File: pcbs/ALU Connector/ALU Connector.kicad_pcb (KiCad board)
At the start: 2 copper layers, 4 parts, among them J101 Conn_02x20_Odd_Even, J102 Conn_02x20_Odd_Even, J103 Conn_01x04, J104 Conn_02x20_Odd_Even

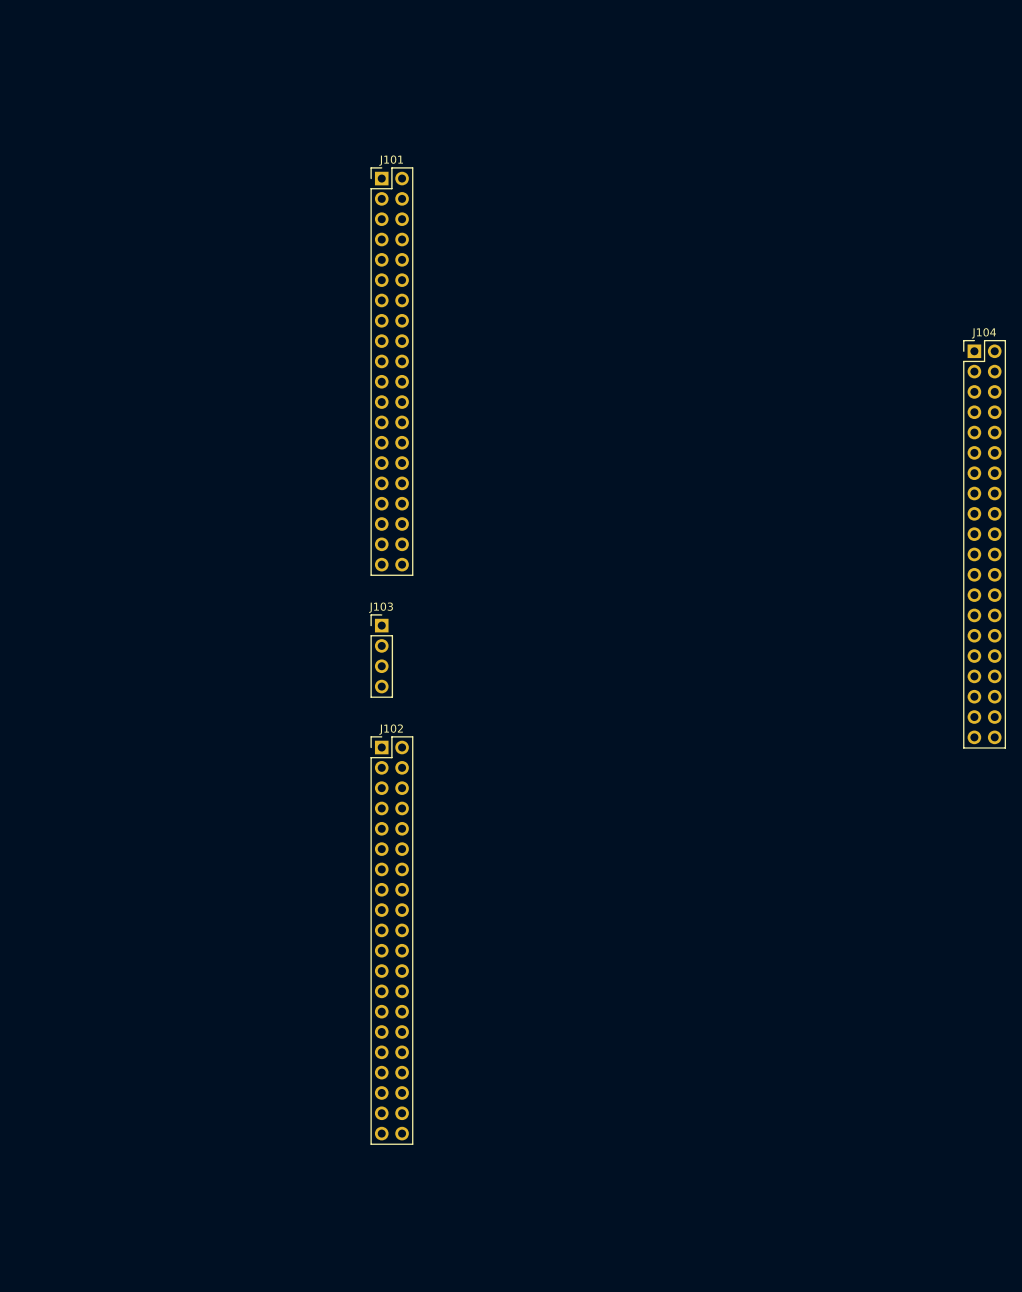
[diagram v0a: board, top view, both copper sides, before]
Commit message: Some basic routing
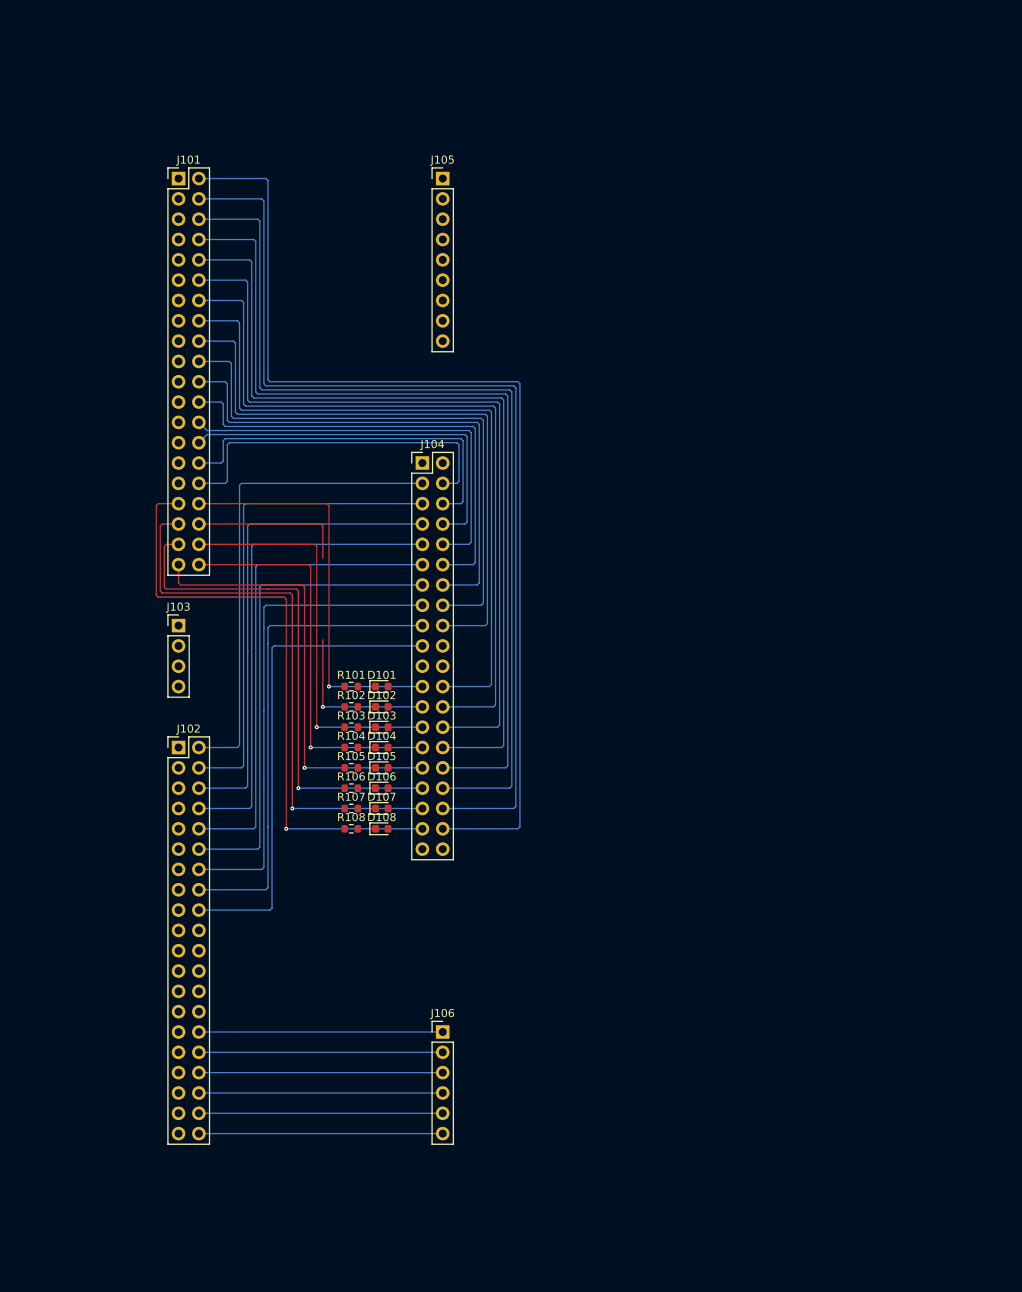
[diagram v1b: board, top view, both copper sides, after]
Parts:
- added D101: Blue, LED_SMD:LED_0603_1608Metric, F.Cu at (76.2, 114.3)
- added D102: Blue, LED_SMD:LED_0603_1608Metric, F.Cu at (76.2, 116.8)
- added D103: Blue, LED_SMD:LED_0603_1608Metric, F.Cu at (76.2, 119.4)
- added D104: Blue, LED_SMD:LED_0603_1608Metric, F.Cu at (76.2, 121.9)
- added D105: Blue, LED_SMD:LED_0603_1608Metric, F.Cu at (76.2, 124.5)
- added D106: Blue, LED_SMD:LED_0603_1608Metric, F.Cu at (76.2, 127.0)
- added D107: Blue, LED_SMD:LED_0603_1608Metric, F.Cu at (76.2, 129.5)
- added D108: Blue, LED_SMD:LED_0603_1608Metric, F.Cu at (76.2, 132.1)
- added J105: Conn_01x09, Connector_PinHeader_2.54mm:PinHeader_1x09_P2.54mm_Vertical, F.Cu at (83.8, 50.8)
- added J106: Conn_01x06, Connector_PinHeader_2.54mm:PinHeader_1x06_P2.54mm_Vertical, F.Cu at (83.8, 157.5)
- added R101: 4k7, Resistor_SMD:R_0603_1608Metric, F.Cu at (72.4, 114.3)
- added R102: 4k7, Resistor_SMD:R_0603_1608Metric, F.Cu at (72.4, 116.8)
- added R103: 4k7, Resistor_SMD:R_0603_1608Metric, F.Cu at (72.4, 119.4)
- added R104: 4k7, Resistor_SMD:R_0603_1608Metric, F.Cu at (72.4, 121.9)
- added R105: 4k7, Resistor_SMD:R_0603_1608Metric, F.Cu at (72.4, 124.5)
- added R106: 4k7, Resistor_SMD:R_0603_1608Metric, F.Cu at (72.4, 127.0)
- added R107: 4k7, Resistor_SMD:R_0603_1608Metric, F.Cu at (72.4, 129.5)
- added R108: 4k7, Resistor_SMD:R_0603_1608Metric, F.Cu at (72.4, 132.1)
- moved J104 70.4 mm to (81.3, 86.4)
- moved J101 25.4 mm to (50.8, 50.8)
- moved J102 25.4 mm to (50.8, 121.9)
- moved J103 25.4 mm to (50.8, 106.7)
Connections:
- J101 pad 10: /A_{4} -> /B_{3}
- J101 pad 12: /A_{5} -> /B_{2}
- J101 pad 14: /A_{6} -> /B_{1}
- J101 pad 16: /A_{7} -> /B_{0}
- J101 pad 18: /B_{0} -> /A_{7}
- J101 pad 2: /A_{0} -> /B_{7}
- J101 pad 20: /B_{1} -> /A_{6}
- J101 pad 22: /B_{2} -> /A_{5}
- J101 pad 24: /B_{3} -> /A_{4}
- J101 pad 26: /B_{4} -> /A_{3}
- J101 pad 28: /B_{5} -> /A_{2}
- J101 pad 30: /B_{6} -> /A_{1}
- J101 pad 32: /B_{7} -> /A_{0}
- J101 pad 33: unconnected-(J101-Pad33) -> /Commit
- J101 pad 34: unconnected-(J101-Pad34) -> /I_{0}
- J101 pad 35: unconnected-(J101-Pad35) -> /Execute
- J101 pad 36: unconnected-(J101-Pad36) -> /I_{1}
- J101 pad 37: unconnected-(J101-Pad37) -> /Decode
- J101 pad 38: unconnected-(J101-Pad38) -> /I_{2}
- J101 pad 39: unconnected-(J101-Pad39) -> /~{SELECT}
- J101 pad 4: /A_{1} -> /B_{6}
- J101 pad 40: unconnected-(J101-Pad40) -> /I_{3}
- J101 pad 6: /A_{2} -> /B_{5}
- J101 pad 8: /A_{3} -> /B_{4}
- J102 pad 1: unconnected-(J102-Pad1) -> /Result_{0}
- J102 pad 10: unconnected-(J102-Pad10) -> /C_{4}
- J102 pad 11: unconnected-(J102-Pad11) -> /Result_{5}
- J102 pad 12: unconnected-(J102-Pad12) -> /C_{5}
- J102 pad 13: unconnected-(J102-Pad13) -> /Result_{6}
- J102 pad 14: unconnected-(J102-Pad14) -> /C_{6}
- J102 pad 15: unconnected-(J102-Pad15) -> /Result_{7}
- J102 pad 16: unconnected-(J102-Pad16) -> /C_{7}
- J102 pad 17: unconnected-(J102-Pad17) -> /Flag
- J102 pad 18: unconnected-(J102-Pad18) -> /DALU_{flag}
- J102 pad 2: unconnected-(J102-Pad2) -> /C_{0}
- J102 pad 3: unconnected-(J102-Pad3) -> /Result_{1}
- J102 pad 30: unconnected-(J102-Pad30) -> /NAND
- J102 pad 32: unconnected-(J102-Pad32) -> /AND
- J102 pad 34: unconnected-(J102-Pad34) -> /XOR
- J102 pad 36: unconnected-(J102-Pad36) -> /OR
- J102 pad 38: unconnected-(J102-Pad38) -> /SUB
- J102 pad 4: unconnected-(J102-Pad4) -> /C_{1}
- J102 pad 40: unconnected-(J102-Pad40) -> /ADD
- J102 pad 5: unconnected-(J102-Pad5) -> /Result_{2}
- J102 pad 6: unconnected-(J102-Pad6) -> /C_{2}
- J102 pad 7: unconnected-(J102-Pad7) -> /Result_{3}
- J102 pad 8: unconnected-(J102-Pad8) -> /C_{3}
- J102 pad 9: unconnected-(J102-Pad9) -> /Result_{4}
- J104 pad 19: unconnected-(J104-Pad19) -> /DALU_{flag}
- J104 pad 23: unconnected-(J104-Pad23) -> /I_{0}
- J104 pad 25: unconnected-(J104-Pad25) -> /I_{1}
- J104 pad 27: unconnected-(J104-Pad27) -> /I_{2}
- J104 pad 29: unconnected-(J104-Pad29) -> /I_{3}
- J104 pad 31: unconnected-(J104-Pad31) -> /~{SELECT}
- J104 pad 33: unconnected-(J104-Pad33) -> /Decode
- J104 pad 35: unconnected-(J104-Pad35) -> /Execute
- J104 pad 37: unconnected-(J104-Pad37) -> /Commit
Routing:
- net /B_{7}: track 0.00 -> 130.5 mm
- net /B_{6}: track 0.00 -> 124.4 mm
- net /B_{5}: track 0.00 -> 118.3 mm
- net /B_{4}: track 0.00 -> 112.2 mm
- net /B_{3}: track 0.00 -> 106.1 mm
- net /B_{2}: track 0.00 -> 100.0 mm
- net /B_{1}: track 0.00 -> 93.9 mm
- net /B_{0}: track 0.00 -> 87.8 mm
- net /A_{7}: track 0.00 -> 76.6 mm
- net /Commit: track 0.00 -> 76.3 mm, vias 0 -> 1
- net /A_{6}: track 0.00 -> 70.5 mm
- net /Execute: track 0.00 -> 70.2 mm, vias 0 -> 1
- net /A_{5}: track 0.00 -> 64.4 mm
- net /Decode: track 0.00 -> 64.1 mm, vias 0 -> 1
- net /C_{2}: track 0.00 -> 60.9 mm
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
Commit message: More routing and LEDs
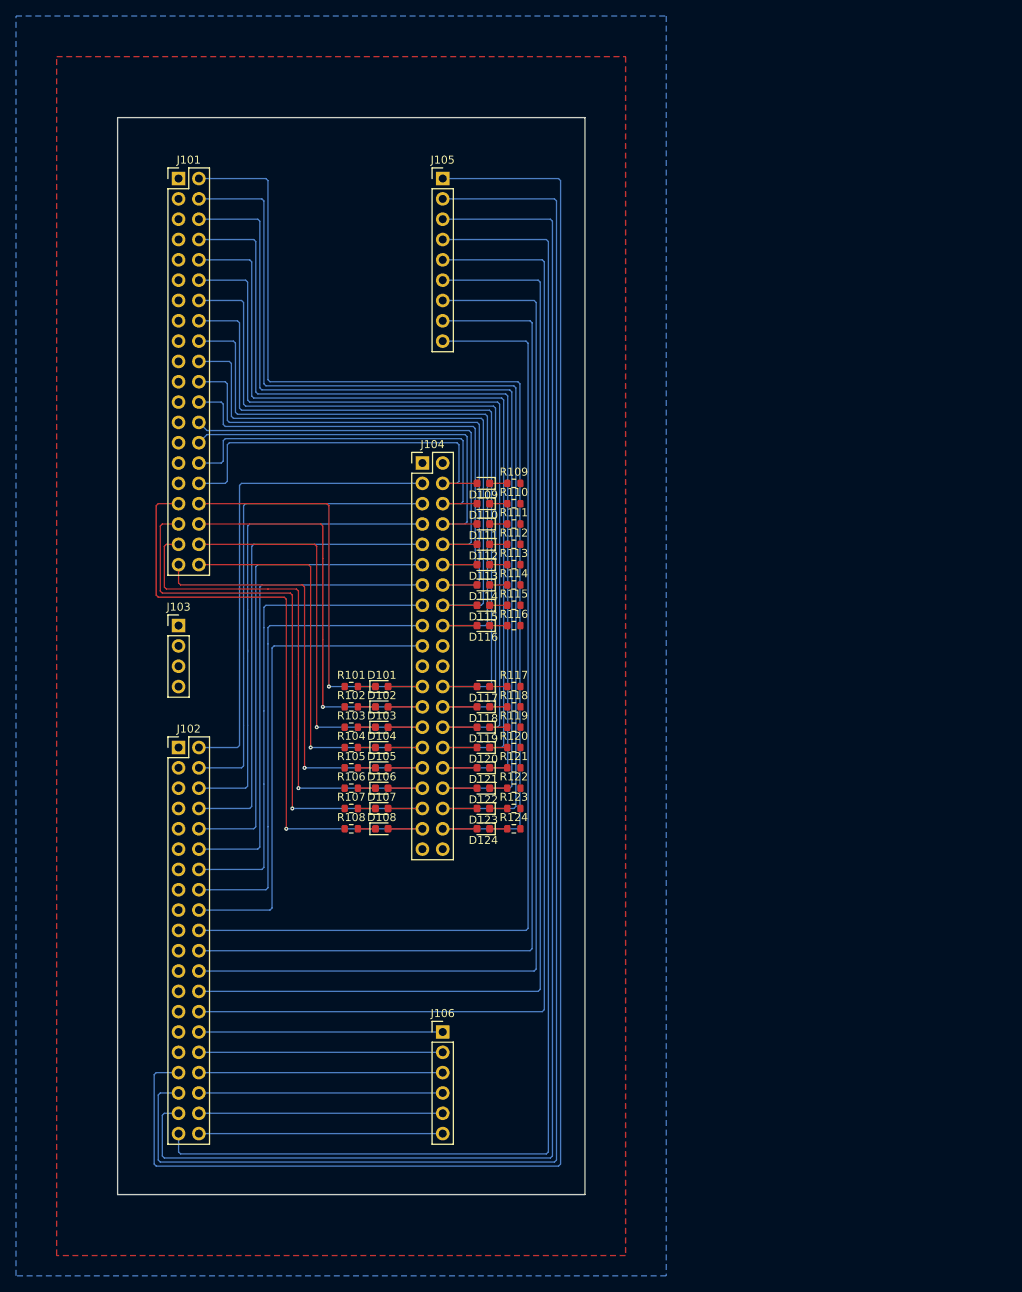
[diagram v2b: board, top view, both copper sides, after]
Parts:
- added D109: Green, LED_SMD:LED_0603_1608Metric, F.Cu at (88.9, 88.9)
- added D110: Green, LED_SMD:LED_0603_1608Metric, F.Cu at (88.9, 91.4)
- added D111: Green, LED_SMD:LED_0603_1608Metric, F.Cu at (88.9, 94.0)
- added D112: Green, LED_SMD:LED_0603_1608Metric, F.Cu at (88.9, 96.5)
- added D113: Green, LED_SMD:LED_0603_1608Metric, F.Cu at (88.9, 99.1)
- added D114: Green, LED_SMD:LED_0603_1608Metric, F.Cu at (88.9, 101.6)
- added D115: Green, LED_SMD:LED_0603_1608Metric, F.Cu at (88.9, 104.1)
- added D116: Green, LED_SMD:LED_0603_1608Metric, F.Cu at (88.9, 106.7)
- added D117: Green, LED_SMD:LED_0603_1608Metric, F.Cu at (88.9, 114.3)
- added D118: Green, LED_SMD:LED_0603_1608Metric, F.Cu at (88.9, 116.8)
- added D119: Green, LED_SMD:LED_0603_1608Metric, F.Cu at (88.9, 119.4)
- added D120: Green, LED_SMD:LED_0603_1608Metric, F.Cu at (88.9, 121.9)
- added D121: Green, LED_SMD:LED_0603_1608Metric, F.Cu at (88.9, 124.5)
- added D122: Green, LED_SMD:LED_0603_1608Metric, F.Cu at (88.9, 127.0)
- added D123: Green, LED_SMD:LED_0603_1608Metric, F.Cu at (88.9, 129.5)
- added D124: Green, LED_SMD:LED_0603_1608Metric, F.Cu at (88.9, 132.1)
- added R109: 4k7, Resistor_SMD:R_0603_1608Metric, F.Cu at (92.7, 88.9)
- added R110: 4k7, Resistor_SMD:R_0603_1608Metric, F.Cu at (92.7, 91.4)
- added R111: 4k7, Resistor_SMD:R_0603_1608Metric, F.Cu at (92.7, 94.0)
- added R112: 4k7, Resistor_SMD:R_0603_1608Metric, F.Cu at (92.7, 96.5)
- added R113: 4k7, Resistor_SMD:R_0603_1608Metric, F.Cu at (92.7, 99.1)
- added R114: 4k7, Resistor_SMD:R_0603_1608Metric, F.Cu at (92.7, 101.6)
- added R115: 4k7, Resistor_SMD:R_0603_1608Metric, F.Cu at (92.7, 104.1)
- added R116: 4k7, Resistor_SMD:R_0603_1608Metric, F.Cu at (92.7, 106.7)
- added R117: 4k7, Resistor_SMD:R_0603_1608Metric, F.Cu at (92.7, 114.3)
- added R118: 4k7, Resistor_SMD:R_0603_1608Metric, F.Cu at (92.7, 116.8)
- added R119: 4k7, Resistor_SMD:R_0603_1608Metric, F.Cu at (92.7, 119.4)
- added R120: 4k7, Resistor_SMD:R_0603_1608Metric, F.Cu at (92.7, 121.9)
- added R121: 4k7, Resistor_SMD:R_0603_1608Metric, F.Cu at (92.7, 124.5)
- added R122: 4k7, Resistor_SMD:R_0603_1608Metric, F.Cu at (92.7, 127.0)
- added R123: 4k7, Resistor_SMD:R_0603_1608Metric, F.Cu at (92.7, 129.5)
- added R124: 4k7, Resistor_SMD:R_0603_1608Metric, F.Cu at (92.7, 132.1)
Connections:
- J102 pad 1: /Result_{0} -> unconnected-(J102-Pad1)
- J102 pad 11: /Result_{5} -> unconnected-(J102-Pad11)
- J102 pad 13: /Result_{6} -> unconnected-(J102-Pad13)
- J102 pad 15: /Result_{7} -> unconnected-(J102-Pad15)
- J102 pad 17: /Flag -> unconnected-(J102-Pad17)
- J102 pad 20: unconnected-(J102-Pad20) -> /Flag
- J102 pad 22: unconnected-(J102-Pad22) -> /Result_{7}
- J102 pad 24: unconnected-(J102-Pad24) -> /Result_{6}
- J102 pad 26: unconnected-(J102-Pad26) -> /Result_{5}
- J102 pad 28: unconnected-(J102-Pad28) -> /Result_{4}
- J102 pad 3: /Result_{1} -> unconnected-(J102-Pad3)
- J102 pad 33: unconnected-(J102-Pad33) -> /Result_{0}
- J102 pad 35: unconnected-(J102-Pad35) -> /Result_{1}
- J102 pad 37: unconnected-(J102-Pad37) -> /Result_{2}
- J102 pad 39: unconnected-(J102-Pad39) -> /Result_{3}
- J102 pad 5: /Result_{2} -> unconnected-(J102-Pad5)
- J102 pad 7: /Result_{3} -> unconnected-(J102-Pad7)
- J102 pad 9: /Result_{4} -> unconnected-(J102-Pad9)
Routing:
- net /Result_{0}: track 0.00 -> 203.1 mm
- net /Result_{1}: track 0.00 -> 195.0 mm
- net /Result_{2}: track 0.00 -> 186.9 mm
- net /Result_{3}: track 0.00 -> 175.8 mm
- net /Result_{4}: track 0.00 -> 149.6 mm
- net /Result_{5}: track 0.00 -> 143.5 mm
- net /Result_{6}: track 0.00 -> 137.4 mm
- net /Result_{7}: track 0.00 -> 131.3 mm
- net /Flag: track 0.00 -> 125.2 mm
- net /I_{1}: track 40.5 -> 54.9 mm
- net /Decode: track 64.1 -> 68.4 mm
- net /B_{7}: track 130.5 -> 134.8 mm
- net /~{SELECT}: track 55.6 -> 59.9 mm
- net /I_{3}: track 50.7 -> 54.9 mm
- net /I_{2}: track 50.7 -> 54.9 mm
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- added copper zone on B.Cu, net +5V
- added copper zone on F.Cu, net GND
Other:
- board outline added: 58.4 x 134.6 mm

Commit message: Realised a mistake
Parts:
- added J107: Conn_01x10, Connector_PinHeader_2.54mm:PinHeader_1x10_P2.54mm_Vertical, F.Cu at (63.5, 170.2)
- J105: value Conn_01x09 -> Conn_01x10; footprint Connector_PinHeader_2.54mm:PinHeader_1x09_P2.54mm_Vertical -> Connector_PinHeader_2.54mm:PinHeader_1x10_P2.54mm_Vertical
- J106: value Conn_01x06 -> Conn_01x10; footprint Connector_PinHeader_2.54mm:PinHeader_1x06_P2.54mm_Vertical -> Connector_PinHeader_2.54mm:PinHeader_1x10_P2.54mm_Vertical
- moved J105 96.2 mm to (63.5, 144.8), turned to 90 degrees
- moved J106 20.3 mm to (63.5, 157.5), turned to 90 degrees
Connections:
- J102 pad 1: unconnected-(J102-Pad1) -> /C_{0}
- J102 pad 10: /C_{4} -> unconnected-(J102-Pad10)
- J102 pad 11: unconnected-(J102-Pad11) -> /In_{08}
- J102 pad 12: /C_{5} -> /In_{09}
- J102 pad 13: unconnected-(J102-Pad13) -> /In_{06}
- J102 pad 14: /C_{6} -> /In_{07}
- J102 pad 15: unconnected-(J102-Pad15) -> /In_{05}
- J102 pad 16: /C_{7} -> /In_{04}
- J102 pad 17: unconnected-(J102-Pad17) -> /In_{03}
- J102 pad 18: /DALU_{flag} -> /In_{02}
- J102 pad 19: unconnected-(J102-Pad19) -> /In_{01}
- J102 pad 2: /C_{0} -> /C_{1}
- J102 pad 20: /Flag -> /In_{00}
- J102 pad 22: /Result_{7} -> unconnected-(J102-Pad22)
- J102 pad 24: /Result_{6} -> unconnected-(J102-Pad24)
- J102 pad 26: /Result_{5} -> unconnected-(J102-Pad26)
- J102 pad 28: /Result_{4} -> unconnected-(J102-Pad28)
- J102 pad 3: unconnected-(J102-Pad3) -> /C_{2}
- J102 pad 30: /NAND -> unconnected-(J102-Pad30)
- J102 pad 32: /AND -> unconnected-(J102-Pad32)
- J102 pad 33: /Result_{0} -> unconnected-(J102-Pad33)
- J102 pad 34: /XOR -> unconnected-(J102-Pad34)
- J102 pad 35: /Result_{1} -> unconnected-(J102-Pad35)
- J102 pad 36: /OR -> unconnected-(J102-Pad36)
- J102 pad 37: /Result_{2} -> unconnected-(J102-Pad37)
- J102 pad 38: /SUB -> unconnected-(J102-Pad38)
- J102 pad 39: /Result_{3} -> unconnected-(J102-Pad39)
- J102 pad 4: /C_{1} -> /C_{3}
- J102 pad 40: /ADD -> unconnected-(J102-Pad40)
- J102 pad 5: unconnected-(J102-Pad5) -> /C_{4}
- J102 pad 6: /C_{2} -> /C_{5}
- J102 pad 7: unconnected-(J102-Pad7) -> /C_{6}
- J102 pad 8: /C_{3} -> /C_{7}
- J102 pad 9: unconnected-(J102-Pad9) -> /DALU_{flag}
- J105 pad 1: /Result_{0} -> /In_{00}
- J105 pad 2: /Result_{1} -> /In_{01}
- J105 pad 3: /Result_{2} -> /In_{02}
- J105 pad 4: /Result_{3} -> /In_{03}
- J105 pad 5: /Result_{4} -> /In_{04}
- J105 pad 6: /Result_{5} -> /In_{05}
- J105 pad 7: /Result_{6} -> /In_{06}
- J105 pad 8: /Result_{7} -> /In_{07}
- J105 pad 9: /Flag -> /In_{08}
- J106 pad 1: /NAND -> unconnected-(J106-Pad1)
- J106 pad 2: /AND -> unconnected-(J106-Pad2)
- J106 pad 3: /XOR -> unconnected-(J106-Pad3)
- J106 pad 4: /OR -> unconnected-(J106-Pad4)
- J106 pad 5: /SUB -> unconnected-(J106-Pad5)
- J106 pad 6: /ADD -> unconnected-(J106-Pad6)
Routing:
- net /Result_{0}: track 203.1 -> 0.00 mm
- net /Result_{1}: track 195.0 -> 0.00 mm
- net /Result_{2}: track 186.9 -> 0.00 mm
- net /Result_{3}: track 175.8 -> 0.00 mm
- net /Result_{4}: track 149.6 -> 0.00 mm
- net /Result_{5}: track 143.5 -> 0.00 mm
- net /Result_{6}: track 137.4 -> 0.00 mm
- net /Result_{7}: track 131.3 -> 0.00 mm
- net /Flag: track 125.2 -> 0.00 mm
- net /In_{09}: track 0.00 -> 42.7 mm
- net /In_{08}: track 0.00 -> 42.6 mm
- net /In_{07}: track 0.00 -> 35.1 mm
- net /In_{06}: track 0.00 -> 35.0 mm
- net /In_{05}: track 0.00 -> 32.7 mm
- net /XOR: track 30.5 -> 0.00 mm
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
